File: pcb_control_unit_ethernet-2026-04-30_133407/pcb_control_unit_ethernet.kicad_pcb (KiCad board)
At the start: 4 copper layers, 188 x 65 mm, 258 parts, among them J1 STDC14, J17 STEP1, J18 STEP2, J2 Micro_SD_Card_Det1, J23 Weight, J3 INB, J30 Valve, J4 DC IN, J5 USB STM32, J6 USB STM32, Q1 IRLML6344, Q2 IRLML6344, Q3 IRLML6344, Q4 MMBT4403, Q5 IRLML6344, Q6 IRLML6344, SW1 Reset, SW2 Boot, U1 STM32H563VITx, U10 SIT3051TK, U11 74AHCT125, U16 24LC512, U2 LAN8742A, U3 DCDC_MP2315, U4 TPS54202DDC, U5 AMS1117-3.3, U6 INA226, U7 TMC2209, U8 TMC2209, U9 HX711, X1 MT3608, Y1 25MHz, Y2 25MHz

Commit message: WIP
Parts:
- removed U3: DCDC_MP2315, liebler_MODULES:DCDC_MP2315
- added C76: u1/35V, Capacitor_SMD:C_0805_2012Metric, F.Cu at (172.2, 106.3)
- added C80: 10u/35V, Capacitor_SMD:C_0805_2012Metric, F.Cu at (172.2, 108.3)
- added C84: u1/16V, Capacitor_SMD:C_0402_1005Metric, F.Cu at (168.3, 103.2)
- added C88: 56p, Capacitor_SMD:C_0402_1005Metric, F.Cu at (173.1, 115.5)
- added C89: 22u, Capacitor_SMD:C_0805_2012Metric, F.Cu at (164.8, 118.0)
- added C98: 22u, Capacitor_SMD:C_0805_2012Metric, F.Cu at (172.2, 118.0)
- added L10: 12uH, Inductor_SMD:L_Abracon_ASPI-0630LR, F.Cu at (168.5, 113.2)
- added R87: 5k1, Resistor_SMD:R_0402_1005Metric, F.Cu at (170.9, 102.5)
- added R88: M1, Resistor_SMD:R_0402_1005Metric, F.Cu at (174.0, 115.5)
- added R96: 330, Resistor_SMD:R_0402_1005Metric, F.Cu at (170.9, 104.4)
- added TP3: PA8, TestPoint:TestPoint_THTPad_D1.0mm_Drill0.5mm, B.Cu at (94.4, 92.7)
- added TP4: PD3, TestPoint:TestPoint_THTPad_D1.0mm_Drill0.5mm, B.Cu at (113.8, 95.0)
- added TP5: PE0, TestPoint:TestPoint_THTPad_D1.0mm_Drill0.5mm, B.Cu at (118.9, 95.0)
- added U12: TPS54202DDC, Package_TO_SOT_SMD:SOT-23-6_Handsoldering, F.Cu at (168.7, 106.3)
- C24, C27: footprint Capacitor_SMD:C_0603_1608Metric -> Capacitor_SMD:C_0805_2012Metric
- C29: footprint Capacitor_SMD:C_0603_1608Metric -> Capacitor_SMD:C_0402_1005Metric
- C36, C37: value u1 -> u1/50V
- C55, C60: footprint Capacitor_SMD:C_0805_2012Metric_Pad1.18x1.45mm_HandSolder -> Capacitor_SMD:C_0805_2012Metric
- C58: value u1 -> 22n/50V
- C77, C78: value 5p6 -> 10p
- L1, L2, L6: value 600R@100M -> 220R@100M
- L3: value 10uH -> 12uH
- L4: footprint Inductor_SMD:L_0805_2012Metric_Pad1.05x1.20mm_HandSolder -> Inductor_SMD:L_0805_2012Metric
- L5, L7, L8, L9: value 220R -> 220R@100M
- R20, R83, R84: value 2k2 -> 3k3
- R67: value 4k7 -> 5k1
- TP1: moved to B.Cu
- U6: footprint Package_SO:VSSOP-10_3x3mm_P0.5mm -> Package_SO:TSSOP-10_3x3mm_P0.5mm
- moved C53 2.95 mm to (163.3, 104.0), turned to 90 degrees
- moved C60 1.60 mm to (160.8, 74.8)
- moved C24 0.80 mm to (136.3, 80.0)
- moved C28 0.39 mm to (73.2, 91.2)
- moved R43 0.34 mm to (117.8, 99.7), turned to -90 degrees
- moved C27 0.24 mm to (75.2, 91.2)
- turned TP1 to 180 degrees
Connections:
- net VALVE renamed VALVE1
- Robot1 pad 2: +9V -> +12V
- U1 pad 67: T1C1 -> Net-(U1-PA8)
- U1 pad 7: PC13 -> ETHERCAT_IRQ
- U1 pad 84: SPI2_CLK_BUT_NOT_NEEDED -> Net-(U1-PD3)
- U1 pad 91: STEPPER_TX -> STEPPER_RX
- U1 pad 92: STEPPER_RX -> STEPPER_TX
- U1 pad 97: PE0 -> Net-(U1-PE0)
- U13 pad 44: unconnected-(U13A-IRQ/LATCH1-Pad44) -> ETHERCAT_IRQ
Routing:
- net ETHERCAT_IRQ: track 0.00 -> 123.8 mm, vias 0 -> 4
- net GND: track 213.2 -> 257.6 mm, vias 516 -> 534
- net /psu/FB12: track 0.00 -> 17.0 mm
- net Net-(U1-PA8): track 0.00 -> 14.3 mm
- net /psu/SW12: track 0.00 -> 14.2 mm, vias 0 -> 2
- net +12V: track 0.00 -> 11.7 mm
- net +9V: track 10.6 -> 0.00 mm
- net 5-24V: track 166.7 -> 174.7 mm, vias 33 -> 32
- net +3V3: track 503.8 -> 507.5 mm
- net I2C1_SCL: track 98.1 -> 94.5 mm
- net STEPPER_RX: track 48.4 -> 51.1 mm
- net I2C1_SDA: track 103.0 -> 100.6 mm
- net Net-(U1-PE0): track 0.00 -> 2.45 mm
- net ROBOT_RX: track 93.6 -> 95.7 mm
- net /psu/BOOT12: track 0.00 -> 1.87 mm
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
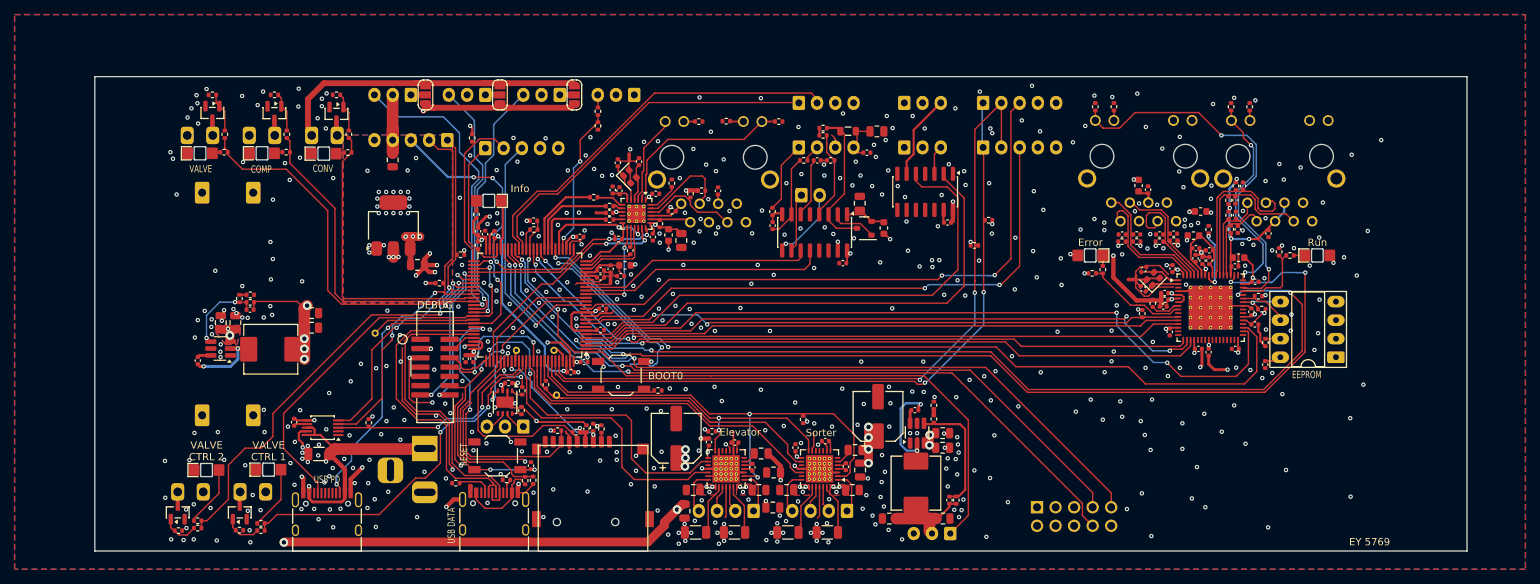
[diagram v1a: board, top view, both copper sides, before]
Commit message: Almost orderable, but: Size is too large to fit
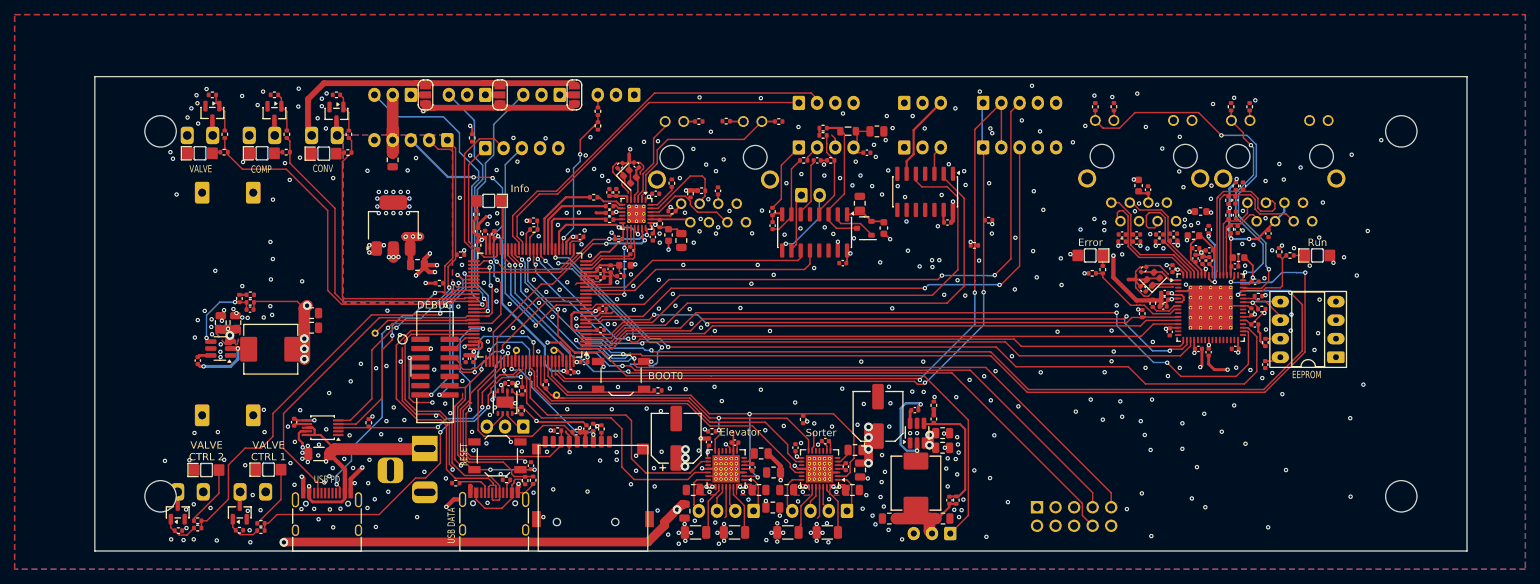
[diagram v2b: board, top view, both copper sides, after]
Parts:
- added H1: MountingHole, MountingHole:MountingHole_4.3mm_M4_DIN965, F.Cu at (235.0, 65.0)
- added H2: MountingHole, MountingHole:MountingHole_4.3mm_M4_DIN965, F.Cu at (235.0, 115.0)
- added H3: MountingHole, MountingHole:MountingHole_4.3mm_M4_DIN965, F.Cu at (65.0, 115.0)
- added H4: MountingHole, MountingHole:MountingHole_4.3mm_M4_DIN965, F.Cu at (65.0, 65.0)
- moved C19 0.57 mm to (130.2, 69.6), turned to 135 degrees
- moved C20 0.57 mm to (126.5, 73.4)
- moved C17 0.50 mm to (128.0, 69.7), turned to 45 degrees
- moved C21 0.49 mm to (127.5, 73.4)
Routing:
- net Net-(C17-Pad2): track 5.96 -> 13.4 mm
- net GND: track 257.6 -> 262.7 mm
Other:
- board text added: "(c) Danielo Miguel (c) Klaus Liebler"
- board text added: "Factory-in-a-Box Control Unit v0.1"
- board text removed: "EY 5769"
